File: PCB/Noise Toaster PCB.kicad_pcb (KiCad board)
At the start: 2 copper layers, 132.1 x 68.6 mm, 138 parts, among them Q1 2N5457, Q10 2N3906, Q2 2N3904, Q3 2N3904, Q4 2N3904, Q5 2N3904, Q6 2N3904, Q7 2N5457, Q8 2N5457, Q9 2N5457, U1 LM324, U2 LM324, U3 LM386, X4 WNS

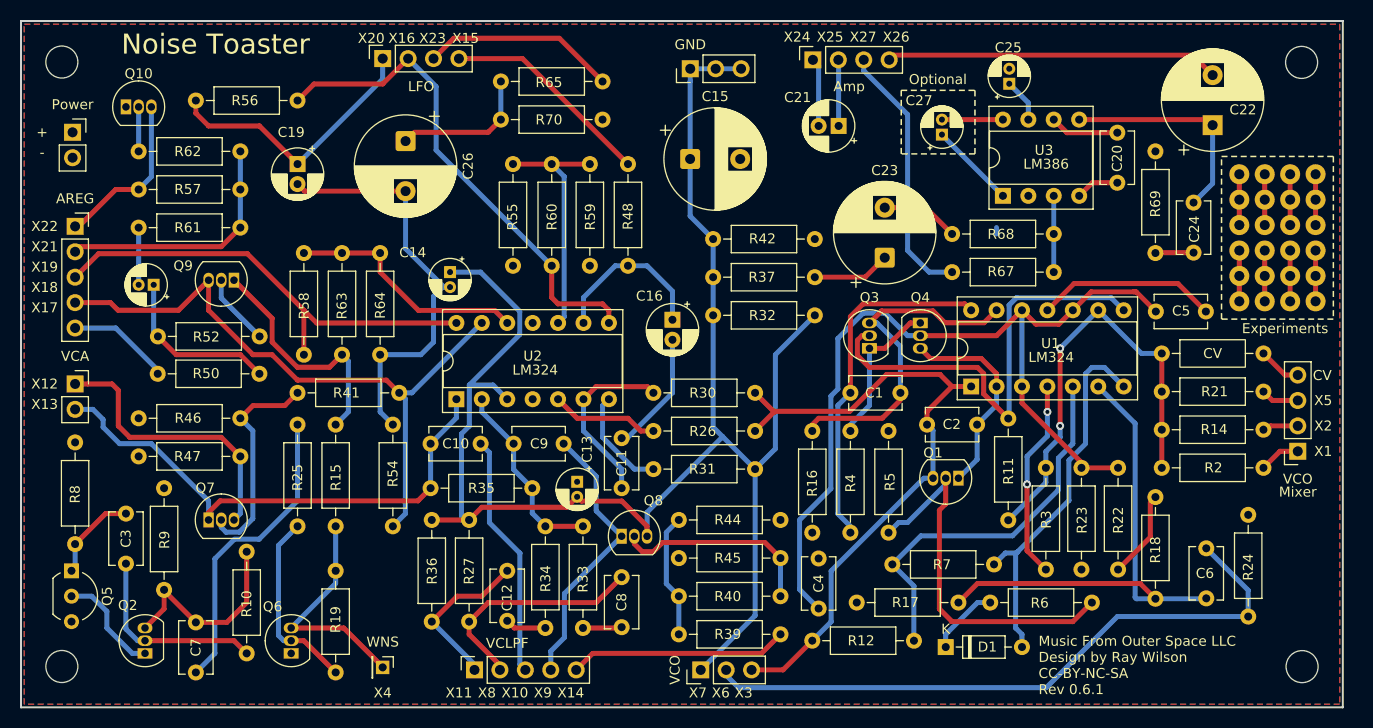
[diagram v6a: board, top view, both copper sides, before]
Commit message: Change TO-92 transistors to wide package to avoid shorting during soldering
Added B- hole for speaker
Added more vias to shorten traces
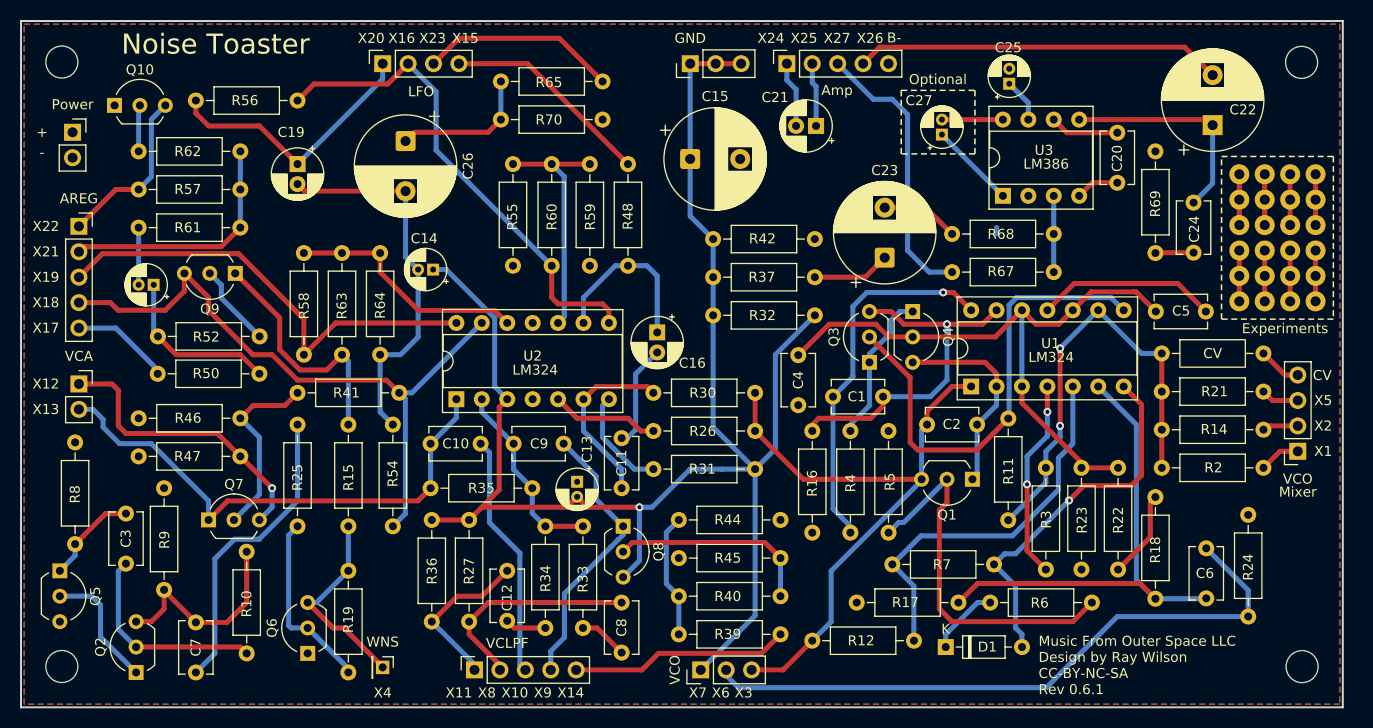
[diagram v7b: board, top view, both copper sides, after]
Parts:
- Amp: footprint Connector_PinSocket_2.54mm:PinSocket_1x04_P2.54mm_Vertical -> Connector_PinSocket_2.54mm:PinSocket_1x05_P2.54mm_Vertical
- Q1, Q10, Q2, Q3, Q4, Q6, Q7, Q8, Q9: footprint Package_TO_SOT_THT:TO-92_Inline -> Package_TO_SOT_THT:TO-92_Inline_Wide
- moved C4 25.4 mm to (152.9, 108.7), turned to -90 degrees
- moved Amp 2.63 mm to (151.8, 79.5)
- moved C8 2.54 mm to (135.3, 133.4)
- moved C21 2.25 mm to (154.7, 85.8)
- moved Q2 2.10 mm to (86.8, 140.4)
- moved C16 1.98 mm to (138.8, 106.4)
- moved C1 1.78 mm to (161.4, 112.8)
- moved C14 1.71 mm to (116.5, 100.1), turned to 180 degrees
- moved Q6 1.65 mm to (103.9, 138.5)
- moved Q1 1.40 mm to (170.3, 121.1)
- moved Q3 1.40 mm to (160.1, 109.4)
- moved Q4 1.37 mm to (164.4, 104.3)
- moved R15 1.27 mm to (108.0, 115.6)
- moved R19 1.27 mm to (108.0, 130.2)
- moved Q5 1.16 mm to (79.2, 130.2)
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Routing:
- net /G2: track 88.8 -> 63.2 mm
- net B-: track 111.2 -> 106.6 mm
- net /RMP: track 66.6 -> 62.8 mm
- net /Audio Amplifier/X26: track 33.3 -> 36.8 mm
- net Net-(Q7-G): track 22.0 -> 18.8 mm
- net GND: track 162.7 -> 159.9 mm, vias 0 -> 1
- net /WNS: track 22.6 -> 19.9 mm
- net Net-(Q3-C): track 32.7 -> 35.2 mm, vias 0 -> 1
- net Net-(Q3-B): track 45.3 -> 47.2 mm
- net /Audio Amplifier/X27: track 26.2 -> 28.0 mm
- net Net-(C1-Pad2): track 34.8 -> 36.6 mm, vias 0 -> 1
- net /Front Panel/X12: track 28.2 -> 29.4 mm, vias 0 -> 1
- net Net-(Q9-G): track 7.20 -> 8.36 mm
- net Net-(U1B--): track 50.9 -> 49.8 mm
- net Net-(C8-Pad2): track 3.78 -> 4.88 mm
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
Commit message: Change 4mm caps to 2mm pitch
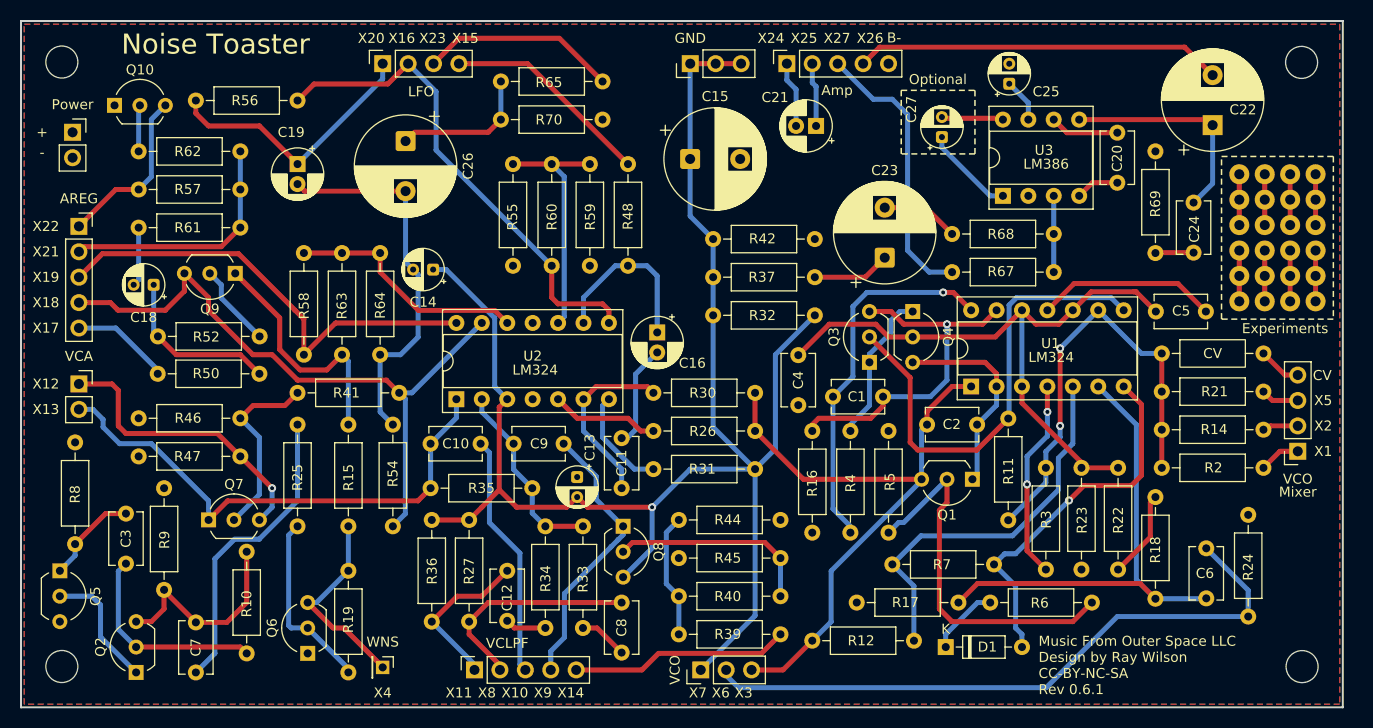
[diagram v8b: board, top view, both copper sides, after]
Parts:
- C13, C14, C18, C25, C27: footprint Capacitor_THT:CP_Radial_D4.0mm_P1.50mm -> Capacitor_THT:CP_Radial_D4.0mm_P2.00mm
- moved C13 0.48 mm to (130.8, 120.8)
- moved C27 0.25 mm to (167.3, 86.9)
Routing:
- net Net-(C27-Pad1): track 8.62 -> 9.14 mm
